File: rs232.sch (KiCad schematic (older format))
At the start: 3 parts, among them U4 MAX3314EEKA-T

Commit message: Get rid of hand-soldering footprints in schematic too
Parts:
- R3: footprint Resistors_SMD:R_0603_HandSoldering -> Resistors_SMD:R_0603
- U4: footprint SOT65P280X145-8N -> MAX3314EEKA-T:SOT65P280X145-8N
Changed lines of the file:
@@
 $Descr A4 11693 8268
 encoding utf-8
-Sheet 4 5
+Sheet 5 5
 Title ""
 Date ""
@@
 F 0 "U4" H 5600 4820 50  0000 C CNN
 F 1 "MAX3314EEKA-T" H 5600 4729 50  0000 C CNN
-F 2 "SOT65P280X145-8N" H 5600 4150 50  0001 L BNN
+F 2 "MAX3314EEKA-T:SOT65P280X145-8N" H 5600 4150 50  0001 L BNN
 F 3 "Maxim Integrated" H 5600 4150 50  0001 L BNN
 F 4 "SOT-23-8 Maxim" H 5600 4150 50  0001 L BNN "Field4"
@@
 F 0 "R3" V 6450 3150 50  0000 C CNN
 F 1 "4k7" V 6550 3150 50  0000 C CNN
-F 2 "Resistors_SMD:R_0603_HandSoldering" V 6580 3150 50  0001 C CNN
+F 2 "Resistors_SMD:R_0603" V 6580 3150 50  0001 C CNN
 F 3 "~" H 6650 3150 50  0001 C CNN
 	1    6650 3150

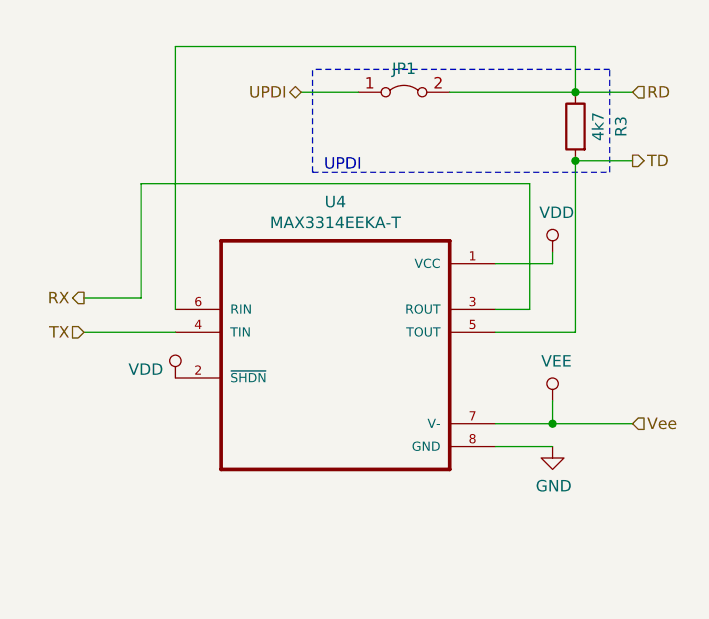
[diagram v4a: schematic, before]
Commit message: Obey some ERC findings
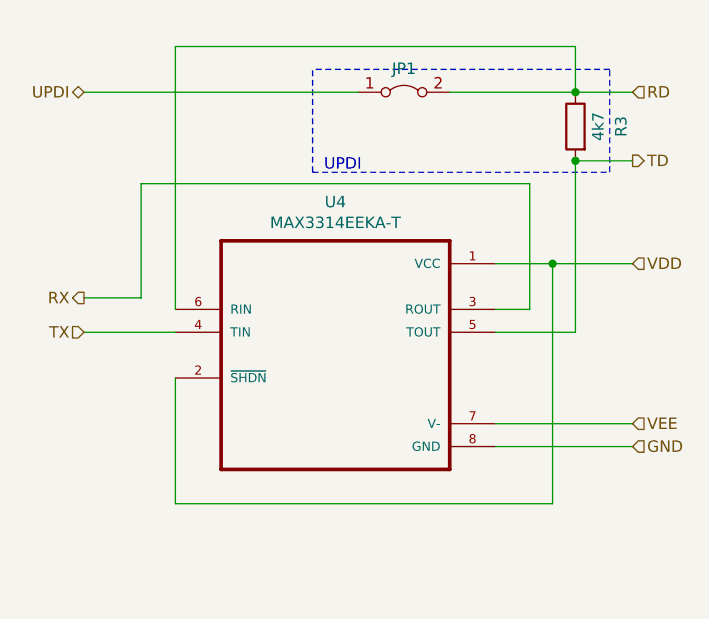
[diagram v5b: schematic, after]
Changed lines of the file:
@@
 Text HLabel 6900 3300 2    50   Output ~ 0
 TD
-$Comp
-L power:VDD #PWR?
-U 1 1 5ED0E3A5
-P 6550 3700
-AR Path="/5ED0E3A5" Ref="#PWR?"  Part="1"
-AR Path="/5ED01473/5ED0E3A5" Ref="#PWR0114"  Part="1"
-F 0 "#PWR0114" H 6550 3550 50  0001 C CNN
-F 1 "VDD" H 6568 3873 50  0000 C CNN
-F 2 "" H 6550 3700 50  0001 C CNN
-F 3 "" H 6550 3700 50  0001 C CNN
-	1    6550 3700
-	1    0    0    -1
-$EndComp
-$Comp
-L power:VEE #PWR?
-U 1 1 5ED0E3AB
-P 6550 4350
-AR Path="/5ED0E3AB" Ref="#PWR?"  Part="1"
-AR Path="/5ED01473/5ED0E3AB" Ref="#PWR0115"  Part="1"
-F 0 "#PWR0115" H 6550 4200 50  0001 C CNN
-F 1 "VEE" H 6567 4523 50  0000 C CNN
-F 2 "" H 6550 4350 50  0001 C CNN
-F 3 "" H 6550 4350 50  0001 C CNN
-	1    6550 4350
-	1    0    0    -1
-$EndComp
 Text HLabel 4500 4050 0    50   Input ~ 0
 TX
 Text HLabel 6900 4450 2    50   Input ~ 0
-Vee
+VEE
 Text HLabel 6900 3000 2    50   Input ~ 0
 RD
-Text HLabel 5450 3000 0    50   BiDi ~ 0
+Text HLabel 4500 3000 0    50   BiDi ~ 0
 UPDI
 Text HLabel 4500 3900 0    50   Output ~ 0
 RX
 Wire Wire Line
-	5450 3000 5700 3000
+	4500 3000 5700 3000
 Wire Wire Line
 	6100 3000 6650 3000
@@
 	5500 3350 5500 2900
 Connection ~ 6650 3000
-$Comp
-L power:GND #PWR?
-U 1 1 5DF382A6
-P 6550 4550
-AR Path="/5DF382A6" Ref="#PWR?"  Part="1"
-AR Path="/5ED01473/5DF382A6" Ref="#PWR0113"  Part="1"
-F 0 "#PWR0113" H 6550 4300 50  0001 C CNN
-F 1 "GND" H 6555 4377 50  0000 C CNN
-F 2 "" H 6550 4550 50  0001 C CNN
-F 3 "" H 6550 4550 50  0001 C CNN
-	1    6550 4550
-	1    0    0    -1
-$EndComp
 $Comp
 L MAX3314EEKA-T:MAX3314EEKA-T U4
@@
 Wire Wire Line
 	4500 4050 4900 4050
+Text HLabel 6900 4550 2    50   Input ~ 0
+GND
+Text HLabel 6900 3750 2    50   Input ~ 0
+VDD
 Wire Wire Line
-	6900 4450 6550 4450
+	6300 4450 6900 4450
 Wire Wire Line
-	6550 4350 6550 4450
-Connection ~ 6550 4450
-Wire Wire Line
-	6550 4450 6300 4450
-Wire Wire Line
-	6550 4550 6300 4550
+	6300 4550 6900 4550
 Wire Wire Line
 	6300 3750 6550 3750
 Wire Wire Line
-	6550 3750 6550 3700
-$Comp
-L power:VDD #PWR?
-U 1 1 5DF679F4
-P 4900 4250
-AR Path="/5DF679F4" Ref="#PWR?"  Part="1"
-AR Path="/5ED01473/5DF679F4" Ref="#PWR0104"  Part="1"
-F 0 "#PWR0104" H 4900 4100 50  0001 C CNN
-F 1 "VDD" H 4847 4287 50  0000 R CNN
-F 2 "" H 4900 4250 50  0001 C CNN
-F 3 "" H 4900 4250 50  0001 C CNN
-	1    4900 4250
-	1    0    0    -1
-$EndComp
+	4900 4250 4900 4800
+Wire Wire Line
+	4900 4800 6550 4800
+Wire Wire Line
+	6550 4800 6550 3750
+Connection ~ 6550 3750
+Wire Wire Line
+	6550 3750 6900 3750
 $EndSCHEMATC

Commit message: Rearrange pins cosmetically
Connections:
- net VDD renamed VCC
- net VEE renamed V-
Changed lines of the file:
@@
 TX
 Text HLabel 6900 4450 2    50   Input ~ 0
-VEE
+V-
 Text HLabel 6900 3000 2    50   Input ~ 0
 RD
@@
 GND
 Text HLabel 6900 3750 2    50   Input ~ 0
-VDD
+VCC
 Wire Wire Line
 	6300 4450 6900 4450
